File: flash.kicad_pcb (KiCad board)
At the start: 2 copper layers, 17.8 x 27.9 mm, 14 parts, among them J1 USB_B_Micro, J2 Conn_01x05, Q1 MMBT2222ALT1G, Q2 MMBT2222ALT1G, U1 CP2102N-A01-GQFN24

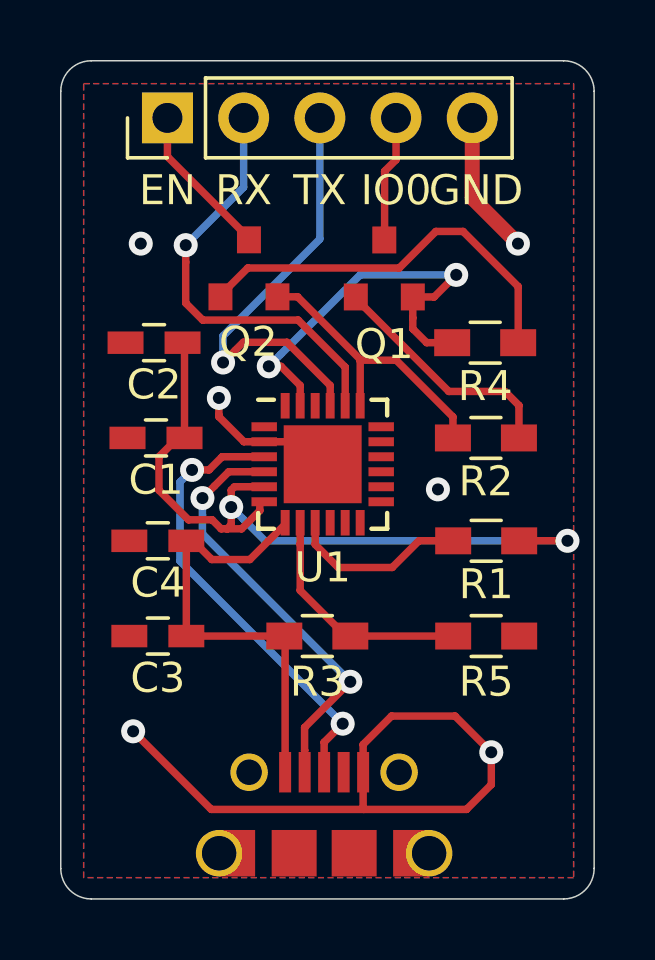
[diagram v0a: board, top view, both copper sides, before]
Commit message: Adjust GND via from header pin
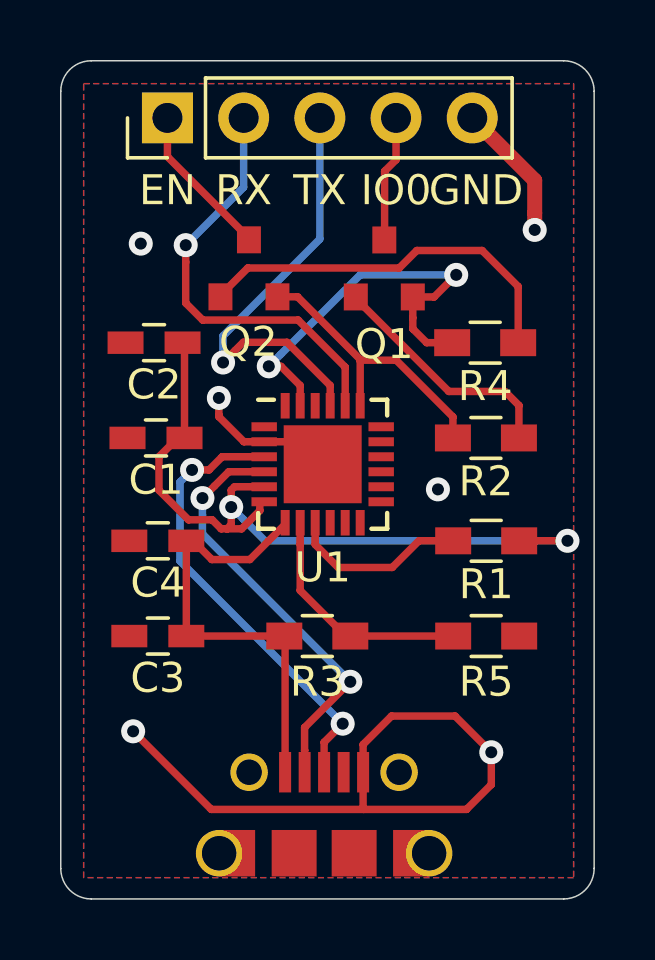
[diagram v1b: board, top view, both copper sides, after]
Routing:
- net Net-(Q2-Pad1): track 13.5 -> 13.0 mm
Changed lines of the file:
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@@
     (thickness 1.6)
     (drawings 19)
-    (tracks 152)
+    (tracks 153)
     (zones 0)
     (modules 14)
@@
   (via (at 147.574 94.0435) (size 0.8) (drill 0.4) (layers F.Cu B.Cu) (net 2))
   (via (at 135.636 93.345) (size 0.8) (drill 0.4) (layers F.Cu B.Cu) (net 2))
-  (segment (start 146.939 72.898) (end 146.939 75.565) (width 0.5) (layer F.Cu) (net 2))
-  (via (at 148.463 77.089) (size 0.8) (drill 0.4) (layers F.Cu B.Cu) (net 2))
-  (segment (start 146.939 75.565) (end 148.463 77.089) (width 0.5) (layer F.Cu) (net 2))
   (via (at 145.796 85.2805) (size 0.8) (drill 0.4) (layers F.Cu B.Cu) (net 2))
   (segment (start 143.302 93.784) (end 144.249 92.837) (width 0.25) (layer F.Cu) (net 2))
@@
   (segment (start 138.4935 82.798183) (end 138.4935 82.232498) (width 0.25) (layer F.Cu) (net 2))
   (via (at 135.89 77.089) (size 0.8) (drill 0.4) (layers F.Cu B.Cu) (net 2))
+  (via (at 149.0218 76.6318) (size 0.8) (drill 0.4) (layers F.Cu B.Cu) (net 2))
+  (segment (start 146.939 72.898) (end 149.0218 74.9808) (width 0.5) (layer F.Cu) (net 2))
+  (segment (start 149.0218 74.9808) (end 149.0218 76.066115) (width 0.5) (layer F.Cu) (net 2))
+  (segment (start 149.0218 76.066115) (end 149.0218 76.6318) (width 0.5) (layer F.Cu) (net 2))
   (segment (start 140.702 90.197) (end 140.675 90.17) (width 0.25) (layer F.Cu) (net 3))
   (segment (start 140.702 94.709) (end 140.702 90.197) (width 0.25) (layer F.Cu) (net 3))
@@
   (segment (start 138.557 78.867) (end 138.557 78.917) (width 0.25) (layer F.Cu) (net 10))
   (segment (start 138.5468 78.812) (end 139.457 77.9018) (width 0.25) (layer F.Cu) (net 10))
+  (segment (start 145.092202 77.3176) (end 147.2692 77.3176) (width 0.25) (layer F.Cu) (net 10))
+  (segment (start 144.508002 77.9018) (end 145.092202 77.3176) (width 0.25) (layer F.Cu) (net 10))
+  (segment (start 148.4708 78.5192) (end 148.4708 80.391) (width 0.25) (layer F.Cu) (net 10))
+  (segment (start 139.457 77.9018) (end 144.508002 77.9018) (width 0.25) (layer F.Cu) (net 10))
+  (segment (start 147.2692 77.3176) (end 148.4708 78.5192) (width 0.25) (layer F.Cu) (net 10))
   (segment (start 138.5468 78.862) (end 138.5468 78.812) (width 0.25) (layer F.Cu) (net 10))
-  (segment (start 144.508002 77.9018) (end 145.727202 76.6826) (width 0.25) (layer F.Cu) (net 10))
-  (segment (start 139.457 77.9018) (end 144.508002 77.9018) (width 0.25) (layer F.Cu) (net 10))
-  (segment (start 145.727202 76.6826) (end 146.6342 76.6826) (width 0.25) (layer F.Cu) (net 10))
-  (segment (start 148.4708 78.5192) (end 148.4708 80.391) (width 0.25) (layer F.Cu) (net 10))
-  (segment (start 146.6342 76.6826) (end 148.4708 78.5192) (width 0.25) (layer F.Cu) (net 10))
   (segment (start 141.704 87.118) (end 142.47 87.884) (width 0.25) (layer F.Cu) (net 11))
   (segment (start 141.704 86.443) (end 141.704 87.118) (width 0.25) (layer F.Cu) (net 11))
